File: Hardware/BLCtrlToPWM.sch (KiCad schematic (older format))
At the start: 38 parts, among them IC1 ATMEGA2560-A, Q1 Q_NMOS_GSD, Q2 Q_NMOS_GSD, Q3 Q_NMOS_GSD, Q4 Q_NMOS_GSD, Q5 Q_NMOS_GSD, Y1 16MHz

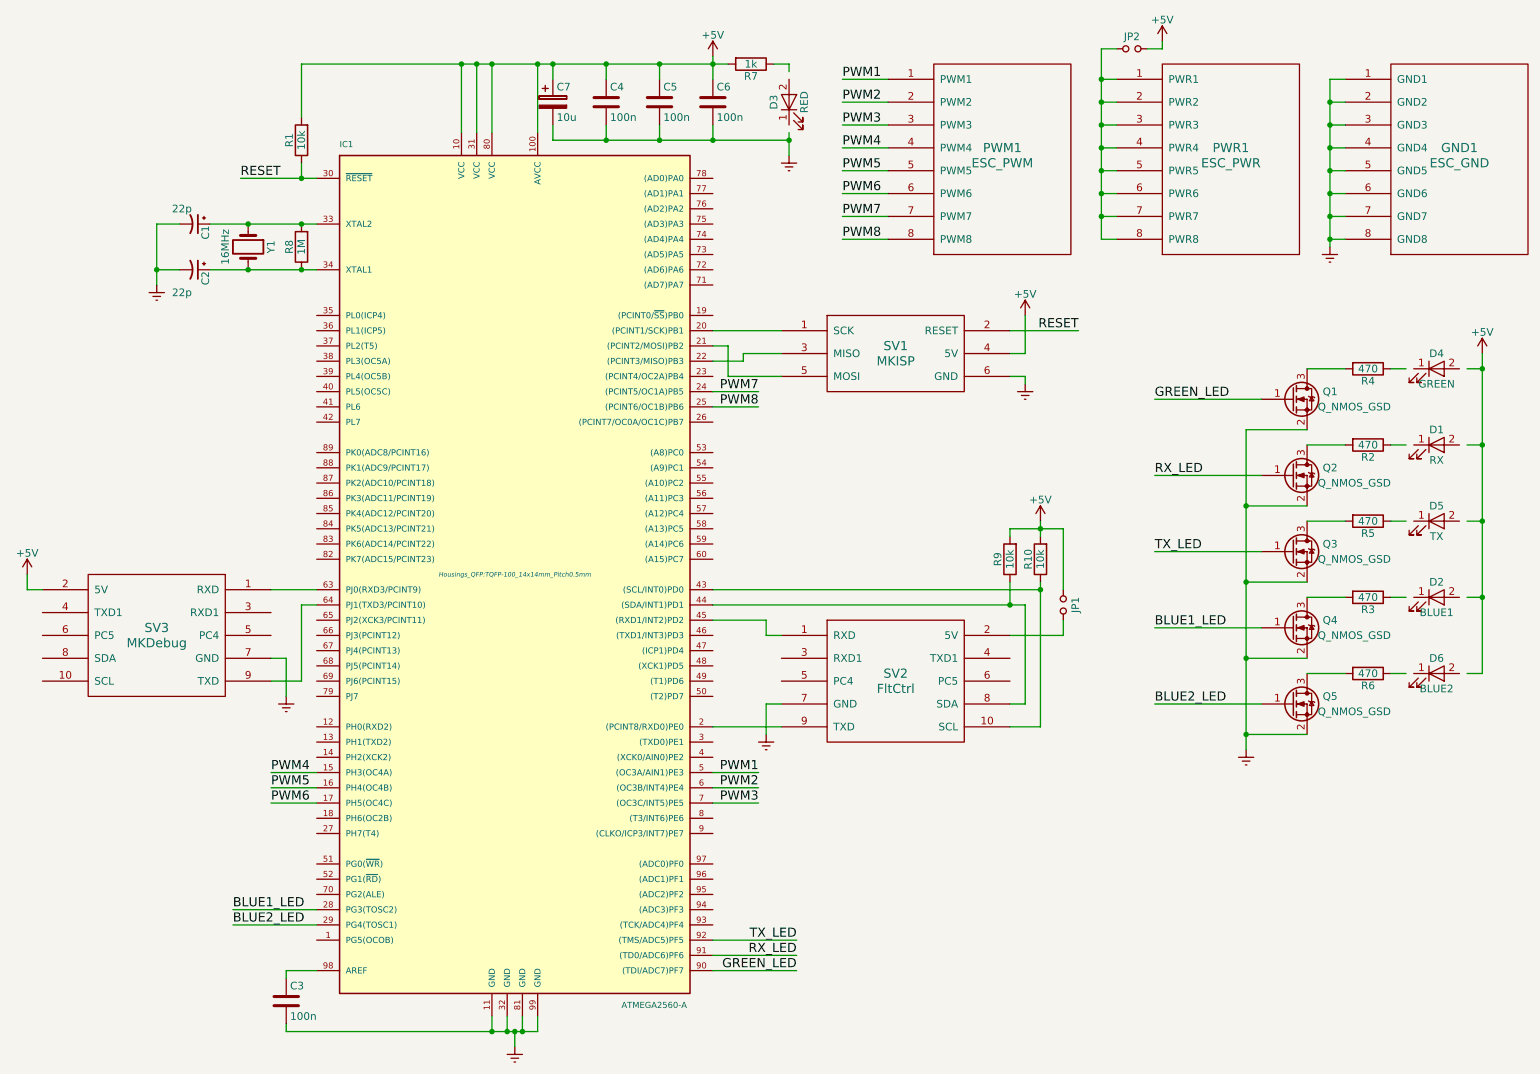
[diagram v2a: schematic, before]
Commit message: Added a side button
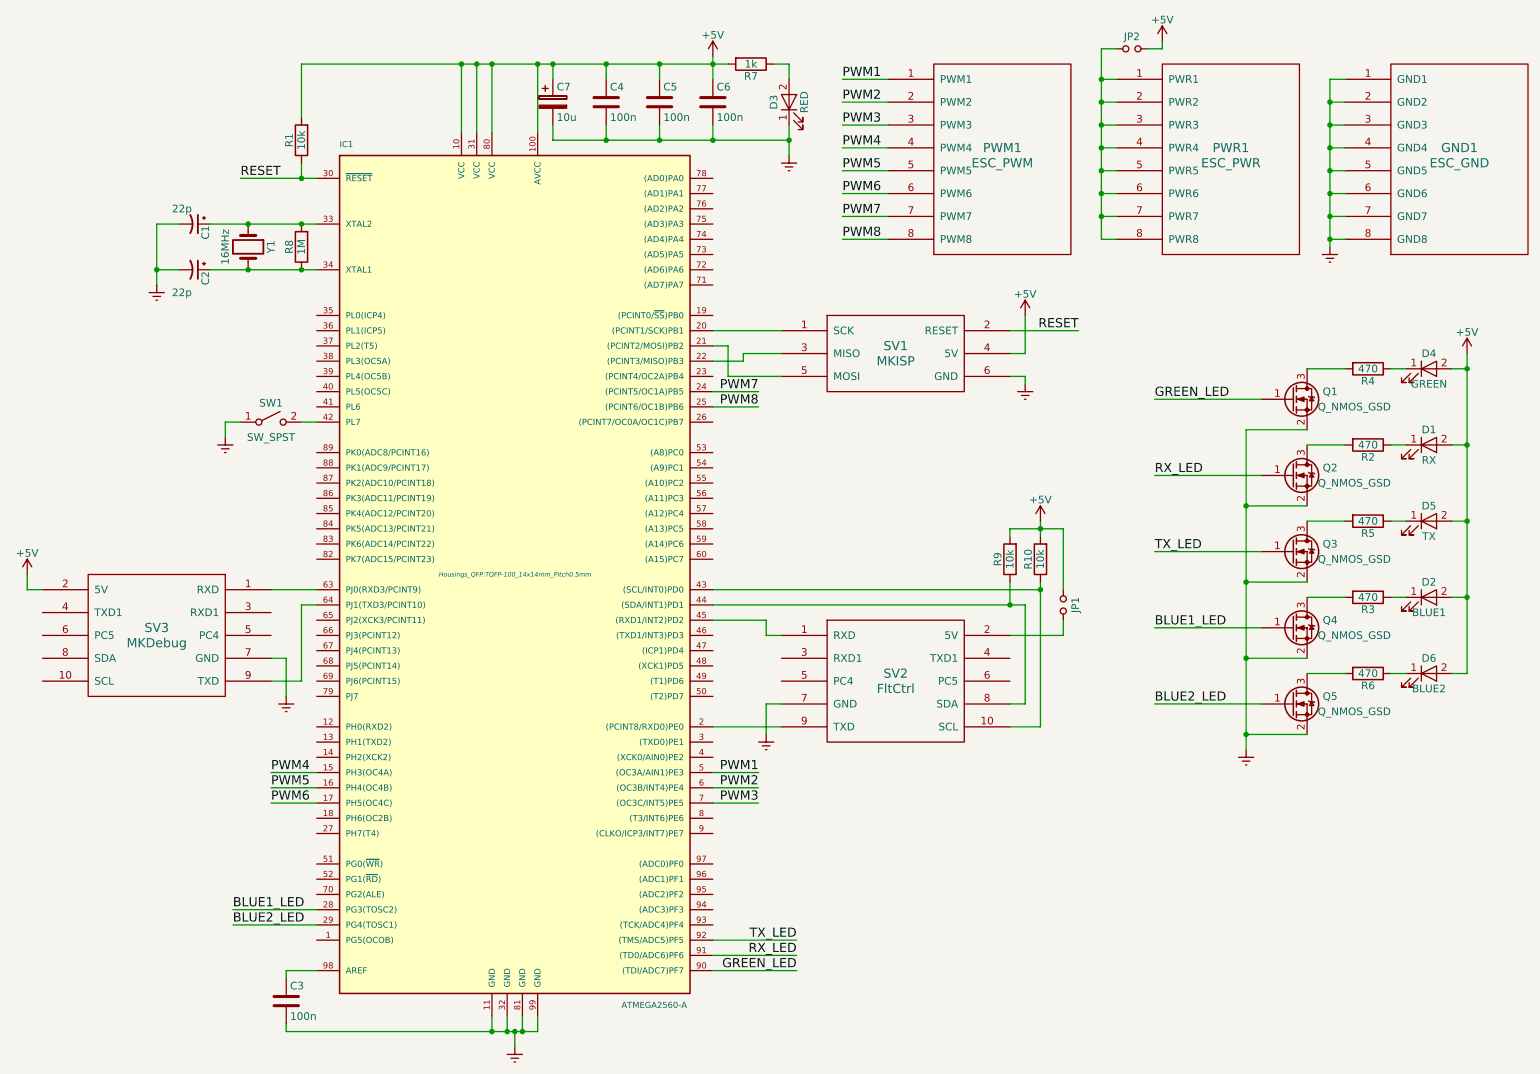
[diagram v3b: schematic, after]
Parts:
- added SW1: SW_SPST, Switches:PanasonicEVQPU_SPST_NO, symbol SW_SPST
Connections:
- wire segments 142 -> 145
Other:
- moved on the sheet: D1, D2, D4, D5, D6
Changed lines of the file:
@@
 EESchema Schematic File Version 2
+LIBS:BLCtrlToPWM-rescue
 LIBS:power
 LIBS:device
@@
 LIBS:mikrokopter
 LIBS:BLCtrlToPWM
+LIBS:switches
 LIBS:BLCtrlToPWM-cache
 EELAYER 25 0
@@
 L LED D1
 U 1 1 56360A2B
-P 10100 3500
-F 0 "D1" H 10100 3600 50  0000 C CNN
-F 1 "RX" H 10100 3400 50  0000 C CNN
-F 2 "LEDs:LED-0805" H 10100 3500 60  0001 C CNN
-F 3 "" H 10100 3500 60  0000 C CNN
-	1    10100 3500
+P 10050 3500
+F 0 "D1" H 10050 3600 50  0000 C CNN
+F 1 "RX" H 10050 3400 50  0000 C CNN
+F 2 "LEDs:LED-0805" H 10050 3500 60  0001 C CNN
+F 3 "" H 10050 3500 60  0000 C CNN
+	1    10050 3500
 	1    0    0    -1
 $EndComp
@@
 L LED D4
 U 1 1 56360A6F
-P 10100 3000
-F 0 "D4" H 10100 3100 50  0000 C CNN
-F 1 "GREEN" H 10100 2900 50  0000 C CNN
-F 2 "LEDs:LED-0805" H 10100 3000 60  0001 C CNN
-F 3 "" H 10100 3000 60  0000 C CNN
-	1    10100 3000
+P 10050 3000
+F 0 "D4" H 10050 3100 50  0000 C CNN
+F 1 "GREEN" H 10050 2900 50  0000 C CNN
+F 2 "LEDs:LED-0805" H 10050 3000 60  0001 C CNN
+F 3 "" H 10050 3000 60  0000 C CNN
+	1    10050 3000
 	1    0    0    -1
 $EndComp
@@
 L LED D5
 U 1 1 56360AB0
-P 10100 4000
-F 0 "D5" H 10100 4100 50  0000 C CNN
-F 1 "TX" H 10100 3900 50  0000 C CNN
-F 2 "LEDs:LED-0805" H 10100 4000 60  0001 C CNN
-F 3 "" H 10100 4000 60  0000 C CNN
-	1    10100 4000
+P 10050 4000
+F 0 "D5" H 10050 4100 50  0000 C CNN
+F 1 "TX" H 10050 3900 50  0000 C CNN
+F 2 "LEDs:LED-0805" H 10050 4000 60  0001 C CNN
+F 3 "" H 10050 4000 60  0000 C CNN
+	1    10050 4000
 	1    0    0    -1
 $EndComp
@@
 L LED D2
 U 1 1 56369996
-P 10100 4500
-F 0 "D2" H 10100 4600 50  0000 C CNN
-F 1 "BLUE1" H 10100 4400 50  0000 C CNN
-F 2 "LEDs:LED-0805" H 10100 4500 60  0001 C CNN
-F 3 "" H 10100 4500 60  0000 C CNN
-	1    10100 4500
+P 10050 4500
+F 0 "D2" H 10050 4600 50  0000 C CNN
+F 1 "BLUE1" H 10050 4400 50  0000 C CNN
+F 2 "LEDs:LED-0805" H 10050 4500 60  0001 C CNN
+F 3 "" H 10050 4500 60  0000 C CNN
+	1    10050 4500
 	1    0    0    -1
 $EndComp
@@
 L LED D6
 U 1 1 563699FA
-P 10100 5000
-F 0 "D6" H 10100 5100 50  0000 C CNN
-F 1 "BLUE2" H 10100 4900 50  0000 C CNN
-F 2 "LEDs:LED-0805" H 10100 5000 60  0001 C CNN
-F 3 "" H 10100 5000 60  0000 C CNN
-	1    10100 5000
+P 10050 5000
+F 0 "D6" H 10050 5100 50  0000 C CNN
+F 1 "BLUE2" H 10050 4900 50  0000 C CNN
+F 2 "LEDs:LED-0805" H 10050 5000 60  0001 C CNN
+F 3 "" H 10050 5000 60  0000 C CNN
+	1    10050 5000
 	1    0    0    -1
 $EndComp
@@
 L +5V #PWR012
 U 1 1 58523055
-P 10400 2900
-F 0 "#PWR012" H 10400 2750 50  0001 C CNN
-F 1 "+5V" H 10400 3040 50  0000 C CNN
-F 2 "" H 10400 2900 60  0000 C CNN
-F 3 "" H 10400 2900 60  0000 C CNN
-	1    10400 2900
+P 10300 2900
+F 0 "#PWR012" H 10300 2750 50  0001 C CNN
+F 1 "+5V" H 10300 3040 50  0000 C CNN
+F 2 "" H 10300 2900 60  0000 C CNN
+F 3 "" H 10300 2900 60  0000 C CNN
+	1    10300 2900
 	1    0    0    -1
 $EndComp
@@
 	0    1    1    0
 $EndComp
+$Comp
+L Jumper_NO_Small JP2
+U 1 1 5852676A
+P 8100 900
+F 0 "JP2" H 8100 980 50  0000 C CNN
+F 1 "Jumper_NO_Small" H 8110 840 50  0001 C CNN
+F 2 "Pin_Headers:Pin_Header_Straight_1x02" H 8100 900 50  0001 C CNN
+F 3 "" H 8100 900 50  0000 C CNN
+	1    8100 900
+	1    0    0    -1
+$EndComp
+$Comp
+L +5V #PWR014
+U 1 1 58526A2E
+P 8300 850
+F 0 "#PWR014" H 8300 700 50  0001 C CNN
+F 1 "+5V" H 8300 990 50  0000 C CNN
+F 2 "" H 8300 850 60  0000 C CNN
+F 3 "" H 8300 850 60  0000 C CNN
+	1    8300 850
+	1    0    0    -1
+$EndComp
+$Comp
+L SW_SPST SW1
+U 1 1 586E43E3
+P 2450 3350
+F 0 "SW1" H 2450 3475 50  0000 C CNN
+F 1 "SW_SPST" H 2450 3250 50  0000 C CNN
+F 2 "Switches:PanasonicEVQPU_SPST_NO" H 2450 3350 50  0001 C CNN
+F 3 "" H 2450 3350 50  0000 C CNN
+	1    2450 3350
+	1    0    0    -1
+$EndComp
+$Comp
+L Earth #PWR015
+U 1 1 586E5143
+P 2150 3450
+F 0 "#PWR015" H 2150 3200 50  0001 C CNN
+F 1 "Earth" H 2150 3300 50  0001 C CNN
+F 2 "" H 2150 3450 60  0000 C CNN
+F 3 "" H 2150 3450 60  0000 C CNN
+	1    2150 3450
+	1    0    0    -1
+$EndComp
 Wire Wire Line
 	2050 2050 2750 2050
@@
 	2550 6950 2550 7000
 Wire Wire Line
-	5850 1000 5850 1050
-Wire Wire Line
-	5850 1450 5850 1600
+	5850 1000 5850 1100
+Wire Wire Line
+	5850 1400 5850 1600
 Wire Wire Line
 	7300 2900 7400 2900
@@
 	7300 4100 7300 4050
 Wire Wire Line
-	10300 3000 10400 3000
-Wire Wire Line
-	10400 3500 10300 3500
-Wire Wire Line
-	10400 4000 10300 4000
-Wire Wire Line
-	10400 4500 10300 4500
-Wire Wire Line
-	10400 5000 10300 5000
+	10200 3000 10300 3000
+Wire Wire Line
+	10300 3500 10200 3500
+Wire Wire Line
+	10300 4000 10200 4000
+Wire Wire Line
+	10300 4500 10200 4500
+Wire Wire Line
+	10300 5000 10200 5000
 Wire Wire Line
 	7400 2900 7400 2650
@@
 	9800 3000 9900 3000
 Wire Wire Line
-	10400 2900 10400 5000
-Connection ~ 10400 4500
-Connection ~ 10400 4000
-Connection ~ 10400 3500
-Connection ~ 10400 3000
+	10300 2900 10300 5000
+Connection ~ 10300 4500
+Connection ~ 10300 4000
+Connection ~ 10300 3500
+Connection ~ 10300 3000
 Wire Wire Line
 	9900 4000 9800 4000
@@
 	7650 4750 7650 4650
 Connection ~ 5850 1500
-$Comp
-L Jumper_NO_Small JP2
-U 1 1 5852676A
-P 8100 900
-F 0 "JP2" H 8100 980 50  0000 C CNN
-F 1 "Jumper_NO_Small" H 8110 840 50  0001 C CNN
-F 2 "Pin_Headers:Pin_Header_Straight_1x02" H 8100 900 50  0001 C CNN
-F 3 "" H 8100 900 50  0000 C CNN
-	1    8100 900
-	1    0    0    -1
-$EndComp
-$Comp
-L +5V #PWR014
-U 1 1 58526A2E
-P 8300 850
-F 0 "#PWR014" H 8300 700 50  0001 C CNN
-F 1 "+5V" H 8300 990 50  0000 C CNN
-F 2 "" H 8300 850 60  0000 C CNN
-F 3 "" H 8300 850 60  0000 C CNN
-	1    8300 850
-	1    0    0    -1
-$EndComp
 Wire Wire Line
 	8200 900  8300 900
@@
 Wire Wire Line
 	5700 4750 5800 4750
+Wire Wire Line
+	2150 3450 2150 3350
+Wire Wire Line
+	2150 3350 2250 3350
+Wire Wire Line
+	2650 3350 2750 3350
 $EndSCHEMATC
